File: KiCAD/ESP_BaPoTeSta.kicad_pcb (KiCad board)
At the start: 2 copper layers, 39.4 x 49.5 mm, 39 parts, among them M3 MountingHole_3.2mm_M3_ISO7380, P1 ProgHdr, P10 CONN_01X04, P13 CONN_01X03, P15 CONN_01X04, P2 Battery, P3 MicroUSB, P4 Flash, P5 Conf, P9 CONN_01X04, Q1 IRLML6302, Q2 BSS806N, U1 MCP1700-330, U2 ESP-12, U3 MCP73831-2-OT, U4 NCP300, U5 ATMEGA328P-A

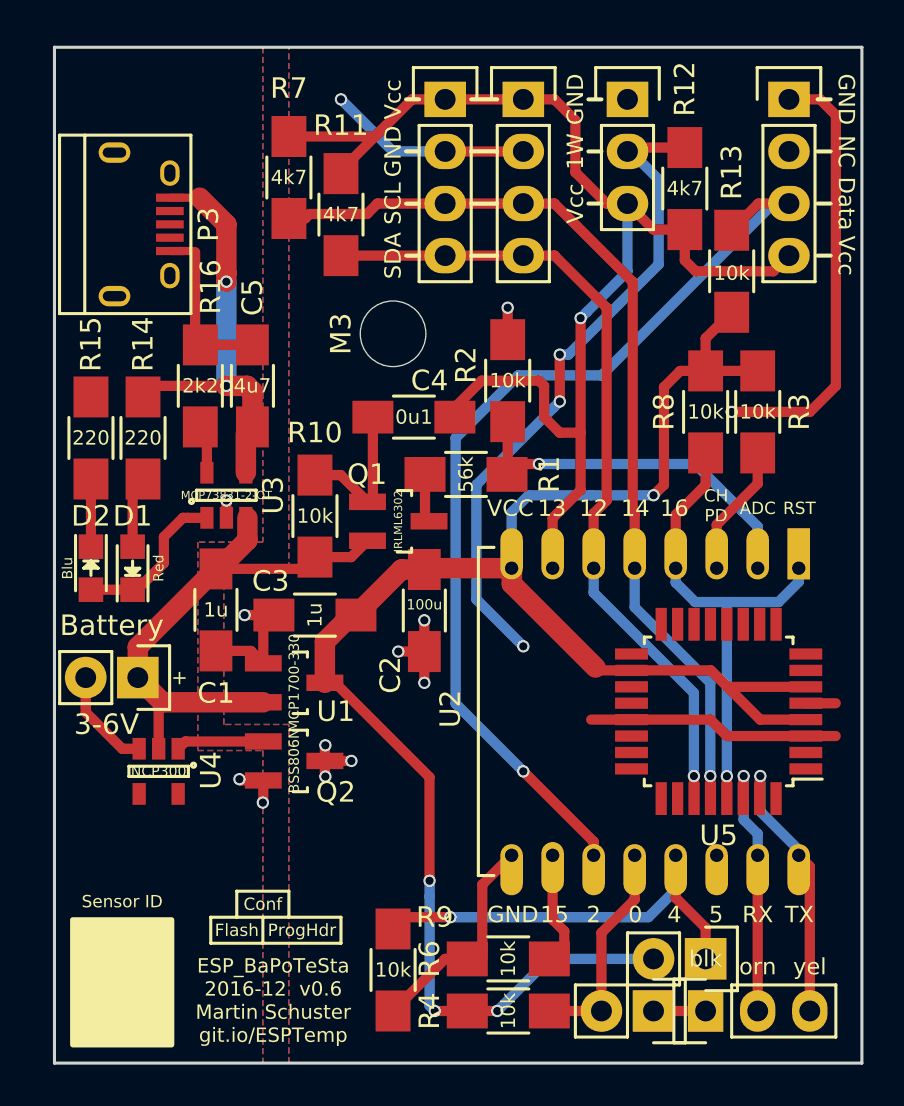
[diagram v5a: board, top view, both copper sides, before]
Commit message: WIP: PCB: Route ATmega
and add some test points
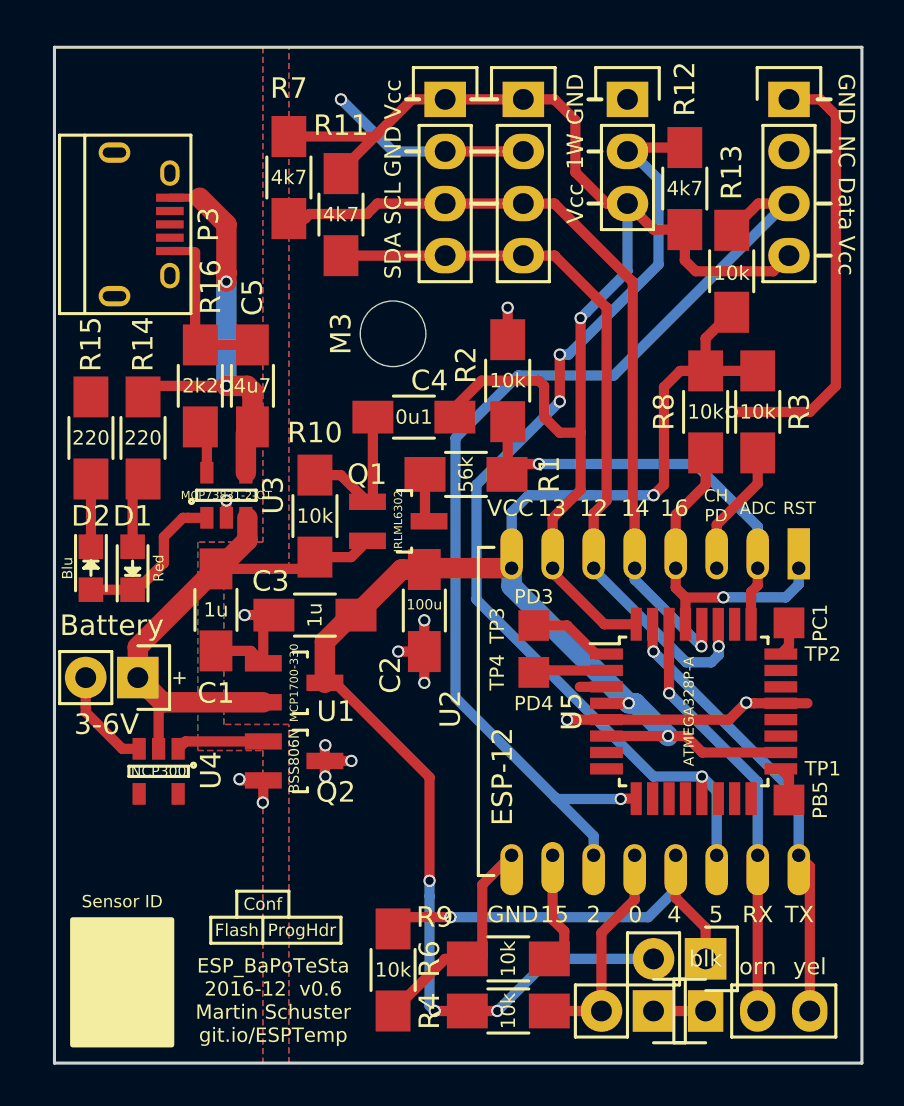
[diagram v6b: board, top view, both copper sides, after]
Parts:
- added TP1: TEST_1P, Measurement_Points:Measurement_Point_Square-SMD-Pad_Small, F.Cu at (159.0, 102.7)
- added TP2: TEST_1P, Measurement_Points:Measurement_Point_Square-SMD-Pad_Small, F.Cu at (159.0, 94.1)
- added TP3: TEST_1P, Measurement_Points:Measurement_Point_Square-SMD-Pad_Small, F.Cu at (146.6, 94.2)
- added TP4: TEST_1P, Measurement_Points:Measurement_Point_Square-SMD-Pad_Small, F.Cu at (146.6, 96.5)
- moved U5 1.22 mm to (154.4, 98.4), turned to 0 degrees
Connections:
- U5 pad 1: (no net) -> /PD3
- U5 pad 13: (no net) -> 1Wire
- U5 pad 17: (no net) -> /PB5
- U5 pad 19: ADC -> (no net)
- U5 pad 2: (no net) -> /PD4
- U5 pad 24: (no net) -> /PC1
- U5 pad 25: (no net) -> ADC
- U5 pad 32: (no net) -> PwrSens
- U5 pad 9: (no net) -> DHTData
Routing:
- net 1Wire: track 32.6 -> 49.2 mm
- net TXD: track 13.6 -> 22.0 mm
- net RST: track 24.0 -> 15.7 mm
- net RXD: track 12.8 -> 20.6 mm
- net SCL: track 45.4 -> 38.9 mm
- net PwrSens: track 63.1 -> 68.5 mm
- net /PD3: track 0.00 -> 4.12 mm
- net DHTData: track 47.6 -> 51.5 mm
- net /PD4: track 0.00 -> 3.59 mm
- net SDA: track 40.2 -> 36.7 mm
- net ADC: track 18.2 -> 21.1 mm
- net /PC1: track 0.00 -> 1.68 mm
- net /PB5: track 0.00 -> 1.68 mm
- net VCC: track 89.0 -> 89.5 mm, vias 4 -> 6
- net GND: track 74.8 -> 74.5 mm, vias 10 -> 12
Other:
- board text added: "PB5"
- board text added: "PC1"
- board text added: "PD3"
- board text added: "PD4"
- board text removed: "1Wire"
- board text removed: "BattVltg"
- board text removed: "Config"
- board text removed: "DHTData"
- board text removed: "Flash"
- board text removed: "PullUp"
- board text removed: "Ser.In"
- board text removed: "Ser.Out"
- board text removed: "WakeUp"

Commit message: DOC: PCB: Add LED documentation
Label pins of connector-legend
Move mounting hole a bit, to make sure the screw won't touch anything
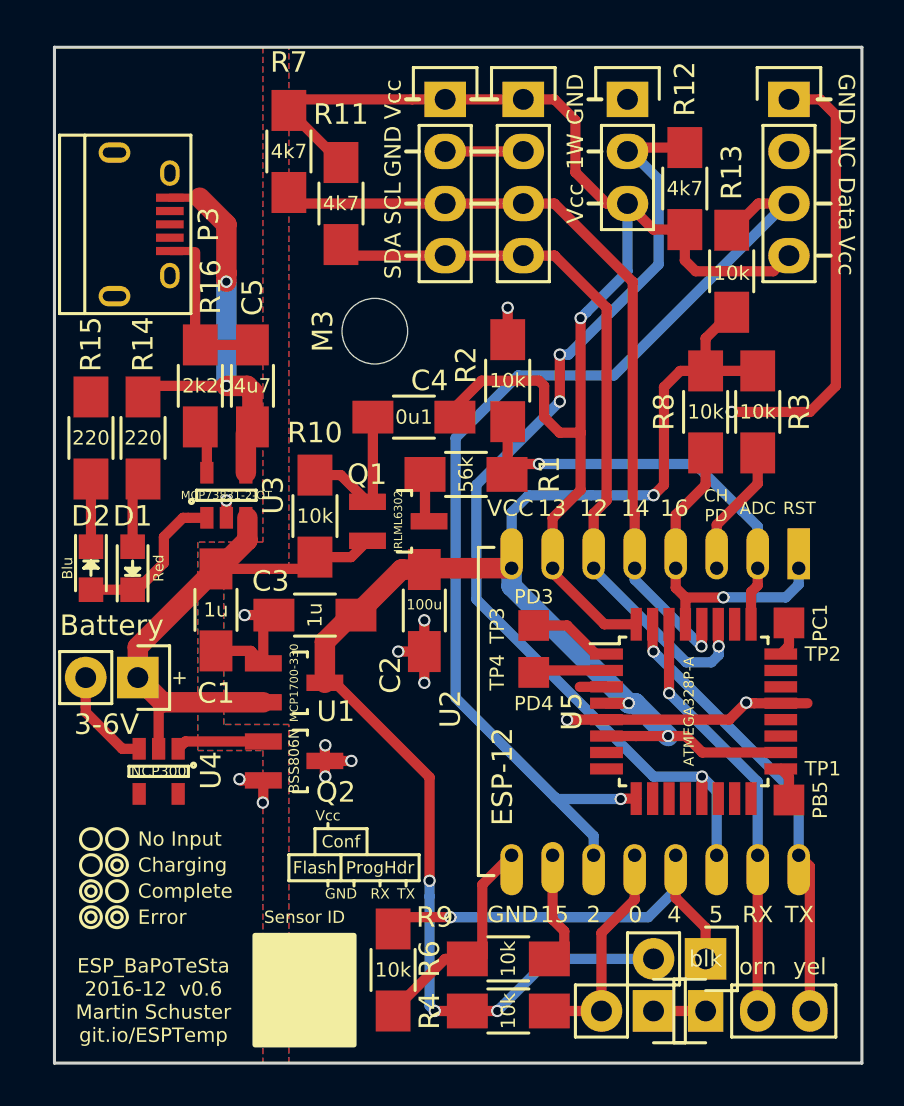
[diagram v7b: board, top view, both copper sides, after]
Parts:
- moved R7 1.27 mm to (134.6, 71.1)
- moved M3 0.90 mm to (138.8, 79.9)
- moved R11 0.54 mm to (137.2, 73.7)
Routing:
- net GND: track 74.5 -> 68.3 mm, vias 12 -> 11
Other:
- board text added: "Charging"
- board text added: "Complete"
- board text added: "Error"
- board text added: "No Input"

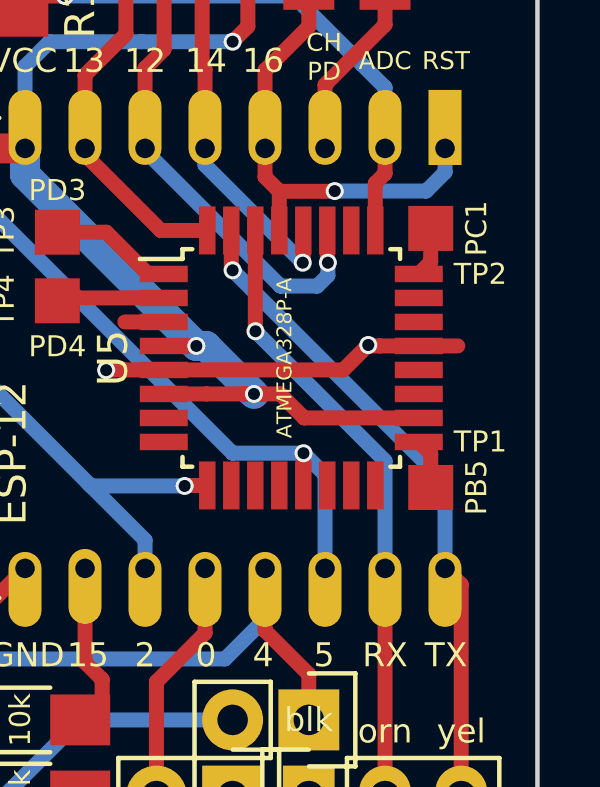
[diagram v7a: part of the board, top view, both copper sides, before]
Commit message: ENH: PCB: Make it easier to attach a 433 sender
Add solder pads for GND and SMD, and move the pads for PB5 and PC1 to
the border of the board

see #34
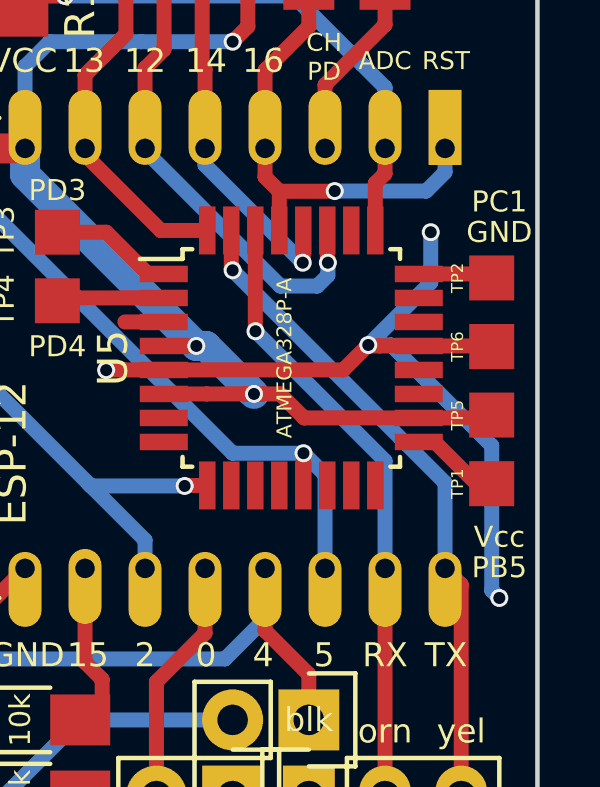
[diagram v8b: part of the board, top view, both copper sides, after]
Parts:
- added TP5: TEST_1P, Measurement_Points:Measurement_Point_Square-SMD-Pad_Small, F.Cu at (161.0, 100.3)
- added TP6: TEST_1P, Measurement_Points:Measurement_Point_Square-SMD-Pad_Small, F.Cu at (161.0, 98.0)
- moved TP2 2.62 mm to (161.0, 95.8)
- moved TP1 2.04 mm to (161.0, 102.6)
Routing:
- net GND: track 68.3 -> 84.8 mm, vias 11 -> 13
- net VCC: track 89.5 -> 92.0 mm
- net /PB5: track 1.68 -> 3.01 mm
- net /PC1: track 1.68 -> 2.49 mm
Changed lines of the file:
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@@
 (kicad_pcb (version 4) (host pcbnew 4.0.2+dfsg1-2~bpo8+1-stable)
   (general
-    (links 100)
+    (links 102)
     (no_connects 1)
     (area 123.114999 65.964999 162.635001 115.645001)
     (thickness 1.6)
-    (drawings 106)
-    (tracks 325)
+    (drawings 108)
+    (tracks 338)
     (zones 0)
-    (modules 43)
+    (modules 45)
     (nets 30)
   )
@@
   )
   (module Measurement_Points:Measurement_Point_Square-SMD-Pad_Small (layer F.Cu)
-    (at 159.004 102.743)
+    (at 161.036 102.616)
     (descr "Mesurement Point, Square, SMD Pad,  1.5mm x 1.5mm,")
     (tags "Mesurement Point Square SMD Pad 1.5x1.5mm")
     (attr virtual)
-    (fp_text reference TP1 (at 1.651 -1.524 180) (layer F.SilkS)
-      (effects (font (size 0.7 0.7) (thickness 0.15)))
+    (fp_text reference TP1 (at -1.143 0 90) (layer F.SilkS)
+      (effects (font (size 0.4 0.4) (thickness 0.1)))
     )
     (fp_text value TEST_1P (at 0 0) (layer F.Fab) hide
@@
   )
   (module Measurement_Points:Measurement_Point_Square-SMD-Pad_Small (layer F.Cu)
-    (at 159.004 94.107)
+    (at 161.036 95.758)
     (descr "Mesurement Point, Square, SMD Pad,  1.5mm x 1.5mm,")
     (tags "Mesurement Point Square SMD Pad 1.5x1.5mm")
     (attr virtual)
-    (fp_text reference TP2 (at 1.651 1.524 180) (layer F.SilkS)
-      (effects (font (size 0.7 0.7) (thickness 0.15)))
+    (fp_text reference TP2 (at -1.143 0 90) (layer F.SilkS)
+      (effects (font (size 0.4 0.4) (thickness 0.1)))
     )
     (fp_text value TEST_1P (at 0 0) (layer F.Fab) hide
@@
     (pad 1 smd rect (at 0 0) (size 1.5 1.5) (layers F.Cu F.Mask)
       (net 29 /PD4))
+  )
+  (module Measurement_Points:Measurement_Point_Square-SMD-Pad_Small (layer F.Cu)
+    (at 161.036 100.33)
+    (descr "Mesurement Point, Square, SMD Pad,  1.5mm x 1.5mm,")
+    (tags "Mesurement Point Square SMD Pad 1.5x1.5mm")
+    (attr virtual)
+    (fp_text reference TP5 (at -1.143 0 90) (layer F.SilkS)
+      (effects (font (size 0.4 0.4) (thickness 0.1)))
+    )
+    (fp_text value TEST_1P (at 0 2) (layer F.Fab)
+      (effects (font (size 1 1) (thickness 0.15)))
+    )
+    (fp_line (start -1 -1) (end 1 -1) (layer F.CrtYd) (width 0.05))
+    (fp_line (start 1 -1) (end 1 1) (layer F.CrtYd) (width 0.05))
+    (fp_line (start 1 1) (end -1 1) (layer F.CrtYd) (width 0.05))
+    (fp_line (start -1 1) (end -1 -1) (layer F.CrtYd) (width 0.05))
+    (pad 1 smd rect (at 0 0) (size 1.5 1.5) (layers F.Cu F.Mask)
+      (net 3 VCC))
+  )
+  (module Measurement_Points:Measurement_Point_Square-SMD-Pad_Small (layer F.Cu)
+    (at 161.036 98.044)
+    (descr "Mesurement Point, Square, SMD Pad,  1.5mm x 1.5mm,")
+    (tags "Mesurement Point Square SMD Pad 1.5x1.5mm")
+    (attr virtual)
+    (fp_text reference TP6 (at -1.143 0 90) (layer F.SilkS)
+      (effects (font (size 0.4 0.4) (thickness 0.1)))
+    )
+    (fp_text value TEST_1P (at 0 2) (layer F.Fab)
+      (effects (font (size 1 1) (thickness 0.15)))
+    )
+    (fp_line (start -1 -1) (end 1 -1) (layer F.CrtYd) (width 0.05))
+    (fp_line (start 1 -1) (end 1 1) (layer F.CrtYd) (width 0.05))
+    (fp_line (start 1 1) (end -1 1) (layer F.CrtYd) (width 0.05))
+    (fp_line (start -1 1) (end -1 -1) (layer F.CrtYd) (width 0.05))
+    (pad 1 smd rect (at 0 0) (size 1.5 1.5) (layers F.Cu F.Mask)
+      (net 2 GND))
+  )
+  (gr_text Vcc (at 161.29 104.394) (layer F.SilkS)
+    (effects (font (size 0.7 0.7) (thickness 0.1)))
+  )
+  (gr_text GND (at 161.29 94.234) (layer F.SilkS)
+    (effects (font (size 0.7 0.7) (thickness 0.1)))
   )
   (gr_text Error (at 127.254 108.458) (layer F.SilkS)
@@
     (effects (font (size 0.5 0.5) (thickness 0.1)))
   )
-  (gr_text PB5 (at 160.528 102.743 90) (layer F.SilkS)
+  (gr_text PB5 (at 161.29 105.41 360) (layer F.SilkS)
     (effects (font (size 0.7 0.7) (thickness 0.1)))
   )
-  (gr_text PC1 (at 160.528 94.107 90) (layer F.SilkS)
+  (gr_text PC1 (at 161.29 93.218 360) (layer F.SilkS)
     (effects (font (size 0.7 0.7) (thickness 0.1)))
   )
@@
   (segment (start 135.89 90.9) (end 137.65686 90.9) (width 0.5) (layer F.Cu) (net 1))
   (segment (start 137.65686 90.9) (end 138.45286 90.104) (width 0.5) (layer F.Cu) (net 1))
+  (segment (start 161.036 104.394) (end 161.036 106.172) (width 0.5) (layer B.Cu) (net 2))
+  (segment (start 161.036 106.172) (end 161.29 106.426) (width 0.5) (layer B.Cu) (net 2))
+  (via (at 161.29 106.426) (size 0.6) (drill 0.4) (layers F.Cu B.Cu) (net 2))
+  (segment (start 159.004 95.9104) (end 159.004 94.234) (width 0.5) (layer B.Cu) (net 2))
+  (segment (start 156.9212 97.9932) (end 159.004 95.9104) (width 0.5) (layer B.Cu) (net 2))
+  (via (at 159.004 94.234) (size 0.6) (drill 0.4) (layers F.Cu B.Cu) (net 2))
+  (segment (start 157.6832 97.9932) (end 161.036 101.346) (width 0.5) (layer B.Cu) (net 2))
+  (segment (start 161.036 101.346) (end 161.036 104.394) (width 0.5) (layer B.Cu) (net 2))
+  (segment (start 156.9212 97.9932) (end 157.6832 97.9932) (width 0.5) (layer B.Cu) (net 2))
+  (segment (start 158.6058 98.025) (end 161.017 98.025) (width 0.5) (layer F.Cu) (net 2))
+  (segment (start 161.017 98.025) (end 161.036 98.044) (width 0.5) (layer F.Cu) (net 2))
   (segment (start 156.9212 97.9932) (end 156.0894 98.825) (width 0.5) (layer F.Cu) (net 2))
   (segment (start 156.0894 98.825) (end 150.1058 98.825) (width 0.5) (layer F.Cu) (net 2))
@@
   (segment (start 150.1058 97.225) (end 148.8058 97.225) (width 0.5) (layer F.Cu) (net 2))
   (segment (start 150.1058 98.825) (end 148.8058 98.825) (width 0.5) (layer F.Cu) (net 2))
-  (segment (start 158.6058 98.025) (end 159.9058 98.025) (width 0.5) (layer F.Cu) (net 2))
   (segment (start 158.6058 98.025) (end 157.3058 98.025) (width 0.5) (layer F.Cu) (net 2))
   (segment (start 136.37514 100.838) (end 137.668 100.838) (width 0.5) (layer F.Cu) (net 2))
@@
   (segment (start 144.05 106.87) (end 145.48 105.44) (width 0.5) (layer F.Cu) (net 2))
   (segment (start 145.48 105.44) (end 145.48 107.06) (width 0.5) (layer F.Cu) (net 2))
+  (segment (start 158.6058 100.425) (end 160.941 100.425) (width 0.5) (layer F.Cu) (net 3))
+  (segment (start 160.941 100.425) (end 161.036 100.33) (width 0.5) (layer F.Cu) (net 3))
   (segment (start 153.0096 99.625) (end 153.1112 99.625) (width 0.5) (layer F.Cu) (net 3))
   (segment (start 153.1112 99.625) (end 153.416 99.625) (width 0.5) (layer F.Cu) (net 3))
@@
   (segment (start 154.94 87.376) (end 153.48 88.836) (width 0.5) (layer F.Cu) (net 25))
   (segment (start 153.48 88.836) (end 153.48 91.44) (width 0.5) (layer F.Cu) (net 25))
-  (segment (start 159.004 101.6232) (end 159.004 102.743) (width 0.5) (layer F.Cu) (net 26))
-  (segment (start 159.004 101.6232) (end 158.6058 101.225) (width 0.5) (layer F.Cu) (net 26))
-  (segment (start 159.004 94.107) (end 159.004 95.2268) (width 0.5) (layer F.Cu) (net 27))
-  (segment (start 159.004 95.2268) (end 158.6058 95.625) (width 0.5) (layer F.Cu) (net 27))
+  (segment (start 158.6058 101.225) (end 159.137 101.225) (width 0.5) (layer F.Cu) (net 26))
+  (segment (start 159.137 101.225) (end 160.528 102.616) (width 0.5) (layer F.Cu) (net 26))
+  (segment (start 160.528 102.616) (end 161.036 102.616) (width 0.5) (layer F.Cu) (net 26))
+  (segment (start 158.6058 95.625) (end 160.903 95.625) (width 0.5) (layer F.Cu) (net 27))
+  (segment (start 160.903 95.625) (end 161.036 95.758) (width 0.5) (layer F.Cu) (net 27))
   (segment (start 146.558 94.234) (end 148.1898 94.234) (width 0.5) (layer F.Cu) (net 28))
   (segment (start 148.1898 94.234) (end 149.5808 95.625) (width 0.5) (layer F.Cu) (net 28))
